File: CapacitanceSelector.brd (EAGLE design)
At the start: 96.5 x 53.5 mm, 12 parts

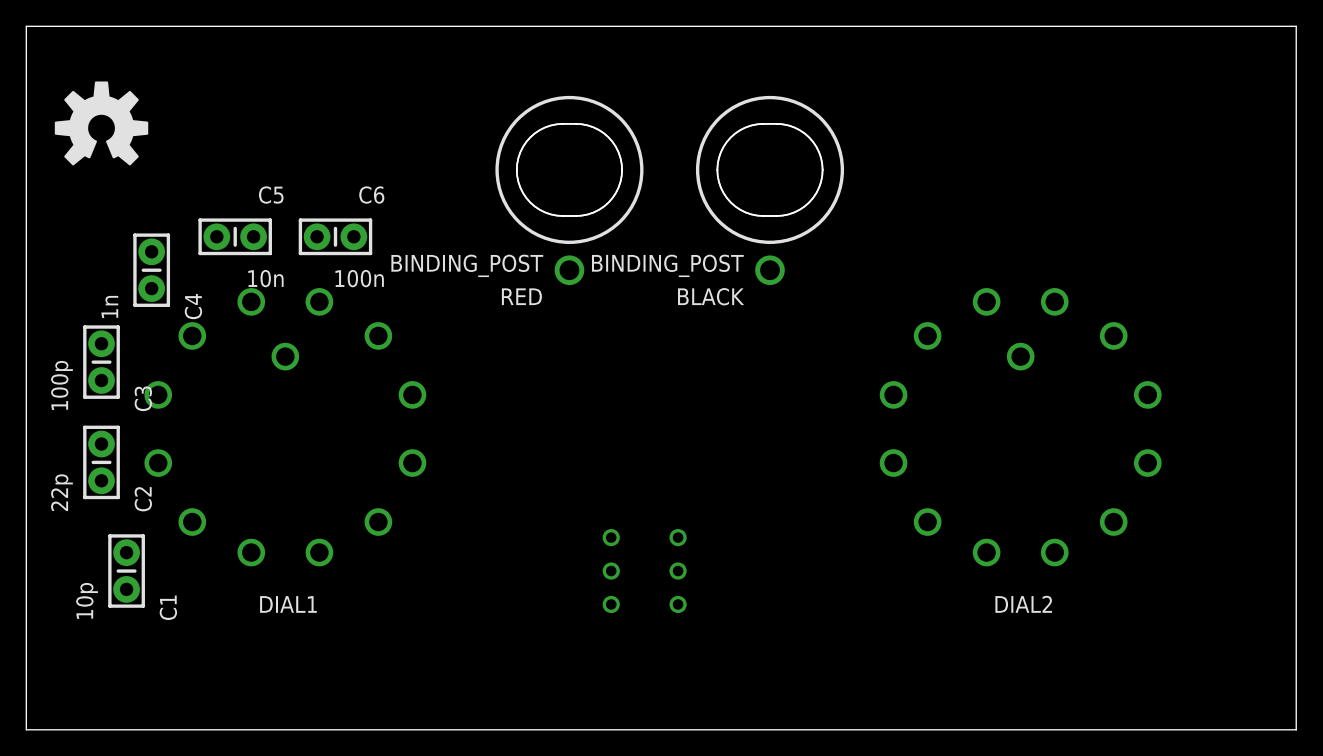
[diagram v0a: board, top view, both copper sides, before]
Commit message: This is going to be an overly expensive board
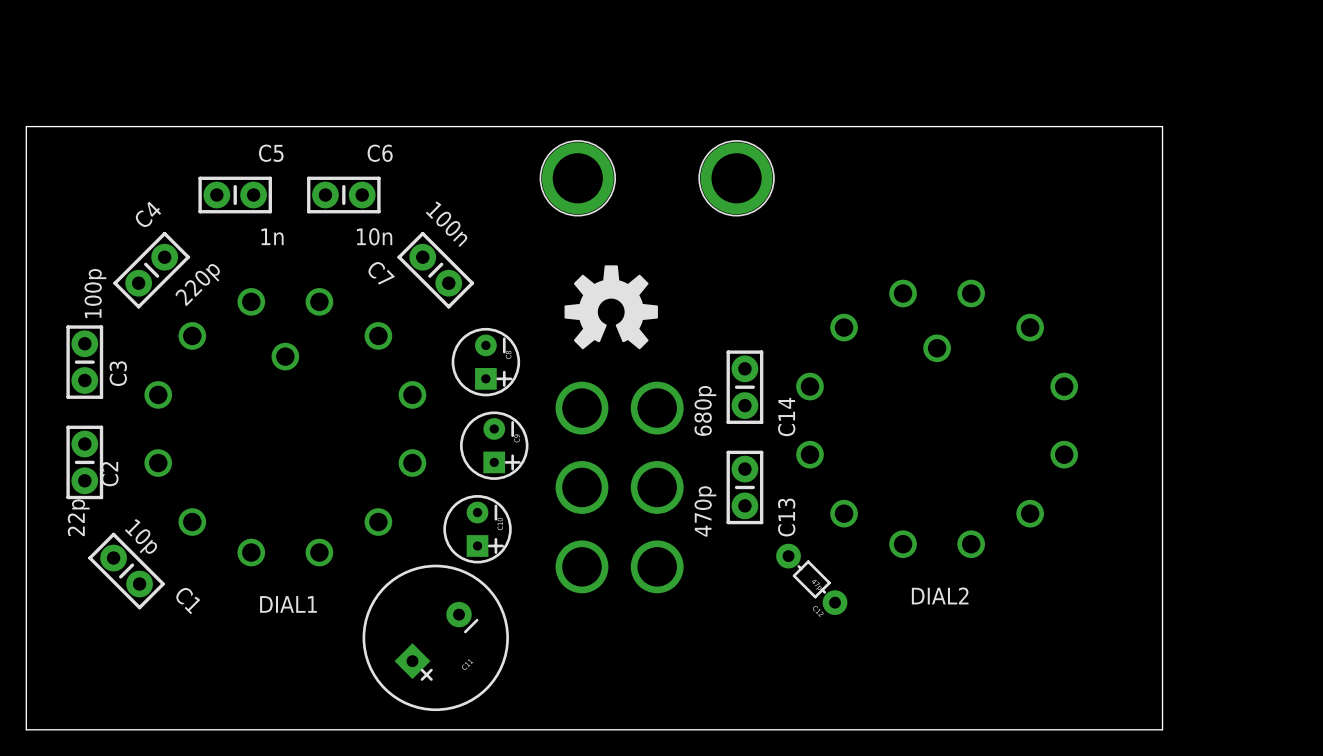
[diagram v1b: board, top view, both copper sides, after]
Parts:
- added C10: 100u, SparkFun-Capacitors:CPOL-RADIAL-10UF-25V-KIT
- added C11: 1000uf/25V, SparkFun-Capacitors:CPOL-RADIAL-1000UF-25V-KIT
- added C12: 47p, SparkFun-Capacitors:AXIAL-5MM
- added C13: 470p, SparkFun-Capacitors:CAP-PTH-SMALL-KIT
- added C14: 680p, SparkFun-Capacitors:CAP-PTH-SMALL-KIT
- added C7: 100n, SparkFun-Capacitors:CAP-PTH-SMALL-KIT
- added C8: 1u, SparkFun-Capacitors:CPOL-RADIAL-10UF-25V-KIT
- added C9: 10u, SparkFun-Capacitors:CPOL-RADIAL-10UF-25V-KIT
- BLACK, RED: value BINDING_POST -> (none); device SparkFun-Connectors:BINDING_POST -> SparkFun-Connectors:BANANA_CONN
- C4: value 1n -> 220p
- C5: value 10n -> 1n
- C6: value 100n -> 10n
- moved LOGO1 41.2 mm to (44.5, 31.8)
- moved U$1 6.63 mm to (45.1, 18.4)
- moved DIAL2 6.38 mm to (69.2, 23.5)
- moved C6 3.24 mm to (24.1, 40.6)
- moved C5 3.17 mm to (15.9, 40.6)
- moved BLACK 2.62 mm to (54.0, 41.9), turned to 0 degrees
- moved C2 1.27 mm to (4.45, 20.3)
- moved C3 1.27 mm to (4.45, 27.9)
- moved RED 0.90 mm to (41.9, 41.9), turned to 0 degrees
- turned C1 to 135 degrees
- turned C4 to 45 degrees
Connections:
- new net N$11: C13.1, DIAL2.3
- new net N$13: C8.1, DIAL1.9
- new net N$14: C12.P$2, C13.2, C14.2
- new net N$15: C14.1, DIAL2.4
- new net N$16: C11.+, DIAL1.12
- new net N$17: C7.2, DIAL1.8
- new net N$2: C12.P$1, DIAL2.2
- new net N$20: C10.1, DIAL1.11
- new net N$21: C9.1, DIAL1.10
- net N$12: now also C10.2, C11.-, C7.1, C8.2, C9.2
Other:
- board size 96.5 x 53.5 mm -> 86.3 x 45.8 mm
